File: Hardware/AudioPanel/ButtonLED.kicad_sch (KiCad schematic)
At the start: 6 parts, among them U19 WS2811

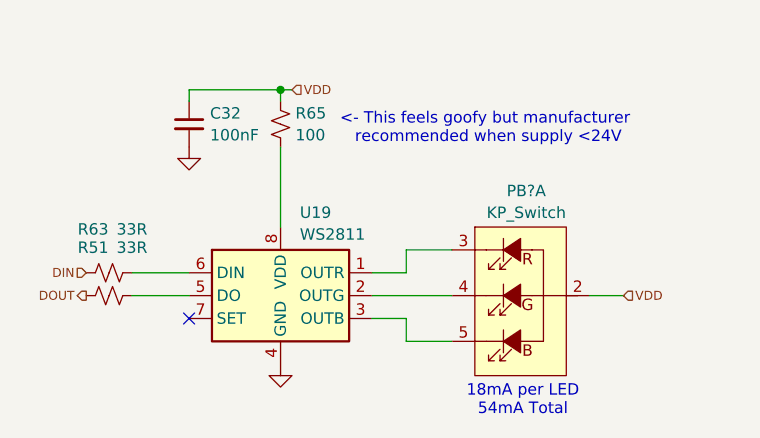
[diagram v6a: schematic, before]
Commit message: Added PCM2904 audio codec
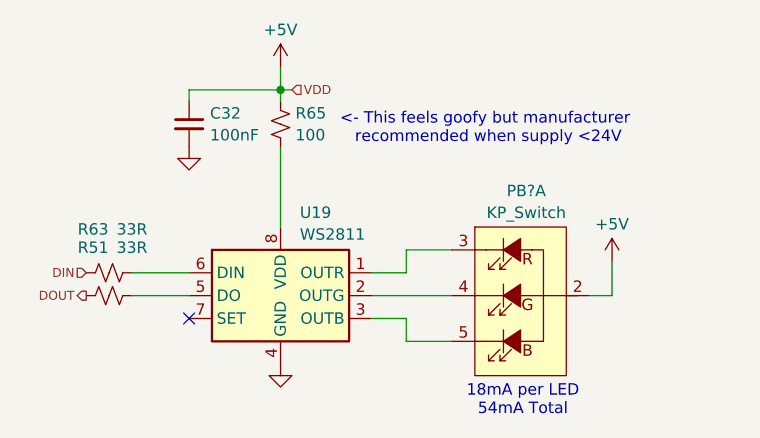
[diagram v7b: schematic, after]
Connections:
- net VDD renamed +5V
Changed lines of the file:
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@@
+	(wire
+		(pts
+			(xy 139.7 66.04) (xy 139.7 68.58)
+		)
+		(stroke
+			(width 0)
+			(type default)
+		)
+	)
 	(wire
 		(pts
@@
 	(wire
 		(pts
+			(xy 176.53 87.63) (xy 176.53 91.44)
+		)
+		(stroke
+			(width 0)
+			(type default)
+		)
+	)
+	(wire
+		(pts
 			(xy 149.86 91.44) (xy 158.75 91.44)
 		)
@@
 	(wire
 		(pts
-			(xy 173.99 91.44) (xy 177.8 91.44)
+			(xy 176.53 91.44) (xy 173.99 91.44)
 		)
 		(stroke
@@
 		(shape input)
 		(at 140.97 68.58 0)
-		(effects
-			(font
-				(size 1 1)
-			)
-			(justify left)
-		)
-	)
-	(hierarchical_label "VDD"
-		(shape input)
-		(at 177.8 91.44 0)
 		(effects
 			(font
@@
 	)
 	(symbol
+		(lib_id "power:+5V")
+		(at 139.7 66.04 0)
+		(unit 1)
+		(exclude_from_sim no)
+		(in_bom yes)
+		(on_board yes)
+		(dnp no)
+		(fields_autoplaced yes)
+		(property "Reference" "#PWR?"
+			(at 139.7 69.85 0)
+			(effects
+				(font
+					(size 1.27 1.27)
+				)
+				(hide yes)
+			)
+		)
+		(property "Value" "+5V"
+			(at 139.7 61.9069 0)
+			(effects
+				(font
+					(size 1.27 1.27)
+				)
+			)
+		)
+		(property "Footprint" ""
+			(at 139.7 66.04 0)
+			(effects
+				(font
+					(size 1.27 1.27)
+				)
+				(hide yes)
+			)
+		)
+		(property "Datasheet" ""
+			(at 139.7 66.04 0)
+			(effects
+				(font
+					(size 1.27 1.27)
+				)
+				(hide yes)
+			)
+		)
+		(property "Description" "Power symbol creates a global label with name \"+5V\""
+			(at 139.7 66.04 0)
+			(effects
+				(font
+					(size 1.27 1.27)
+				)
+				(hide yes)
+			)
+		)
+		(pin "1"
+		)
+		(instances
+			(project "PilotAudioPanel"
+				(path "/2de36a1b-eee5-458c-8325-256a7162eff5/a5cce8a2-fa1f-45df-8605-c295d18be7f1/087c1b72-25ed-41f0-acdd-4665839c97ce"
+					(reference "#PWR079")
+					(unit 1)
+				)
+				(path "/2de36a1b-eee5-458c-8325-256a7162eff5/a5cce8a2-fa1f-45df-8605-c295d18be7f1/0d672bb0-5c3c-47db-9d26-ada4d5a94edf"
+					(reference "#PWR?")
+					(unit 1)
+				)
+				(path "/2de36a1b-eee5-458c-8325-256a7162eff5/a5cce8a2-fa1f-45df-8605-c295d18be7f1/12425dc7-ab06-4bff-804a-d650a7ab7f2f"
+					(reference "#PWR095")
+					(unit 1)
+				)
+				(path "/2de36a1b-eee5-458c-8325-256a7162eff5/a5cce8a2-fa1f-45df-8605-c295d18be7f1/390c3102-f6c6-464a-abca-49d3743e5737"
+					(reference "#PWR091")
+					(unit 1)
+				)
+				(path "/2de36a1b-eee5-458c-8325-256a7162eff5/a5cce8a2-fa1f-45df-8605-c295d18be7f1/3c1c4f7e-9d2a-4715-83bc-474e02a2363b"
+					(reference "#PWR071")
+					(unit 1)
+				)
+				(path "/2de36a1b-eee5-458c-8325-256a7162eff5/a5cce8a2-fa1f-45df-8605-c295d18be7f1/45f10693-960d-407b-bcdb-44cffc888f0e"
+					(reference "#PWR099")
+					(unit 1)
+				)
+				(path "/2de36a1b-eee5-458c-8325-256a7162eff5/a5cce8a2-fa1f-45df-8605-c295d18be7f1/511f6806-7072-4fc6-ba0e-840605abf478"
+					(reference "#PWR083")
+					(unit 1)
+				)
+				(path "/2de36a1b-eee5-458c-8325-256a7162eff5/a5cce8a2-fa1f-45df-8605-c295d18be7f1/5c9bf123-f1c8-4a1f-b808-ac6ee42c4937"
+					(reference "#PWR068")
+					(unit 1)
+				)
+				(path "/2de36a1b-eee5-458c-8325-256a7162eff5/a5cce8a2-fa1f-45df-8605-c295d18be7f1/954c0d67-c94b-4af7-816f-200e052b64c9"
+					(reference "#PWR087")
+					(unit 1)
+				)
+				(path "/2de36a1b-eee5-458c-8325-256a7162eff5/a5cce8a2-fa1f-45df-8605-c295d18be7f1/d2501b73-7727-43e9-a80b-16f0f6fed20b"
+					(reference "#PWR0103")
+					(unit 1)
+				)
+				(path "/2de36a1b-eee5-458c-8325-256a7162eff5/a5cce8a2-fa1f-45df-8605-c295d18be7f1/d7b85838-5187-411c-b5da-a623aecf8ad2"
+					(reference "#PWR075")
+					(unit 1)
+				)
+				(path "/2de36a1b-eee5-458c-8325-256a7162eff5/a5cce8a2-fa1f-45df-8605-c295d18be7f1/fb3ef425-4387-410f-8202-5f46898723c5"
+					(reference "#PWR0107")
+					(unit 1)
+				)
+			)
+		)
+	)
+	(symbol
 		(lib_id "Device:R_Small_US")
 		(at 120.65 91.44 90)
@@
 					(unit 1)
 				)
+			)
+		)
+	)
+	(symbol
+		(lib_id "power:+5V")
+		(at 176.53 87.63 0)
+		(unit 1)
+		(exclude_from_sim no)
+		(in_bom yes)
+		(on_board yes)
+		(dnp no)
+		(fields_autoplaced yes)
+		(property "Reference" "#PWR064"
+			(at 176.53 91.44 0)
+			(effects
+				(font
+					(size 1.27 1.27)
+				)
+				(hide yes)
+			)
+		)
+		(property "Value" "+5V"
+			(at 176.53 83.4969 0)
+			(effects
+				(font
+					(size 1.27 1.27)
+				)
+			)
+		)
+		(property "Footprint" ""
+			(at 176.53 87.63 0)
+			(effects
+				(font
+					(size 1.27 1.27)
+				)
+				(hide yes)
+			)
+		)
+		(property "Datasheet" ""
+			(at 176.53 87.63 0)
+			(effects
+				(font
+					(size 1.27 1.27)
+				)
+				(hide yes)
+			)
+		)
+		(property "Description" "Power symbol creates a global label with name \"+5V\""
+			(at 176.53 87.63 0)
+			(effects
+				(font
+					(size 1.27 1.27)
+				)
+				(hide yes)
+			)
+		)
+		(pin "1"
+		)
+		(instances
+			(project "PilotAudioPanel"
+				(path "/2de36a1b-eee5-458c-8325-256a7162eff5/a5cce8a2-fa1f-45df-8605-c295d18be7f1/087c1b72-25ed-41f0-acdd-4665839c97ce"
+					(reference "#PWR081")
+					(unit 1)
+				)
+				(path "/2de36a1b-eee5-458c-8325-256a7162eff5/a5cce8a2-fa1f-45df-8605-c295d18be7f1/0d672bb0-5c3c-47db-9d26-ada4d5a94edf"
+					(reference "#PWR064")
+					(unit 1)
+				)
+				(path "/2de36a1b-eee5-458c-8325-256a7162eff5/a5cce8a2-fa1f-45df-8605-c295d18be7f1/12425dc7-ab06-4bff-804a-d650a7ab7f2f"
+					(reference "#PWR097")
+					(unit 1)
+				)
+				(path "/2de36a1b-eee5-458c-8325-256a7162eff5/a5cce8a2-fa1f-45df-8605-c295d18be7f1/390c3102-f6c6-464a-abca-49d3743e5737"
+					(reference "#PWR093")
+					(unit 1)
+				)
+				(path "/2de36a1b-eee5-458c-8325-256a7162eff5/a5cce8a2-fa1f-45df-8605-c295d18be7f1/3c1c4f7e-9d2a-4715-83bc-474e02a2363b"
+					(reference "#PWR073")
+					(unit 1)
+				)
+				(path "/2de36a1b-eee5-458c-8325-256a7162eff5/a5cce8a2-fa1f-45df-8605-c295d18be7f1/45f10693-960d-407b-bcdb-44cffc888f0e"
+					(reference "#PWR0101")
+					(unit 1)
+				)
+				(path "/2de36a1b-eee5-458c-8325-256a7162eff5/a5cce8a2-fa1f-45df-8605-c295d18be7f1/511f6806-7072-4fc6-ba0e-840605abf478"
+					(reference "#PWR085")
+					(unit 1)
+				)
+				(path "/2de36a1b-eee5-458c-8325-256a7162eff5/a5cce8a2-fa1f-45df-8605-c295d18be7f1/5c9bf123-f1c8-4a1f-b808-ac6ee42c4937"
+					(reference "#PWR069")
+					(unit 1)
+				)
+				(path "/2de36a1b-eee5-458c-8325-256a7162eff5/a5cce8a2-fa1f-45df-8605-c295d18be7f1/954c0d67-c94b-4af7-816f-200e052b64c9"
+					(reference "#PWR089")
+					(unit 1)
+				)
+				(path "/2de36a1b-eee5-458c-8325-256a7162eff5/a5cce8a2-fa1f-45df-8605-c295d18be7f1/d2501b73-7727-43e9-a80b-16f0f6fed20b"
+					(reference "#PWR0105")
+					(unit 1)
+				)
+				(path "/2de36a1b-eee5-458c-8325-256a7162eff5/a5cce8a2-fa1f-45df-8605-c295d18be7f1/d7b85838-5187-411c-b5da-a623aecf8ad2"
+					(reference "#PWR077")
+					(unit 1)
+				)
+				(path "/2de36a1b-eee5-458c-8325-256a7162eff5/a5cce8a2-fa1f-45df-8605-c295d18be7f1/fb3ef425-4387-410f-8202-5f46898723c5"
+					(reference "#PWR0109")
+					(unit 1)
+				)
